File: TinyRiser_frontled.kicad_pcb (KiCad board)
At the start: 4 copper layers, 113.2 x 23.5 mm, 33 parts, among them J2 Bus_PCI_Express_x16, J3 Bus_M.2_Socket_M, J5 Conn_02x04_Odd_Even, M1 Fan_4pin

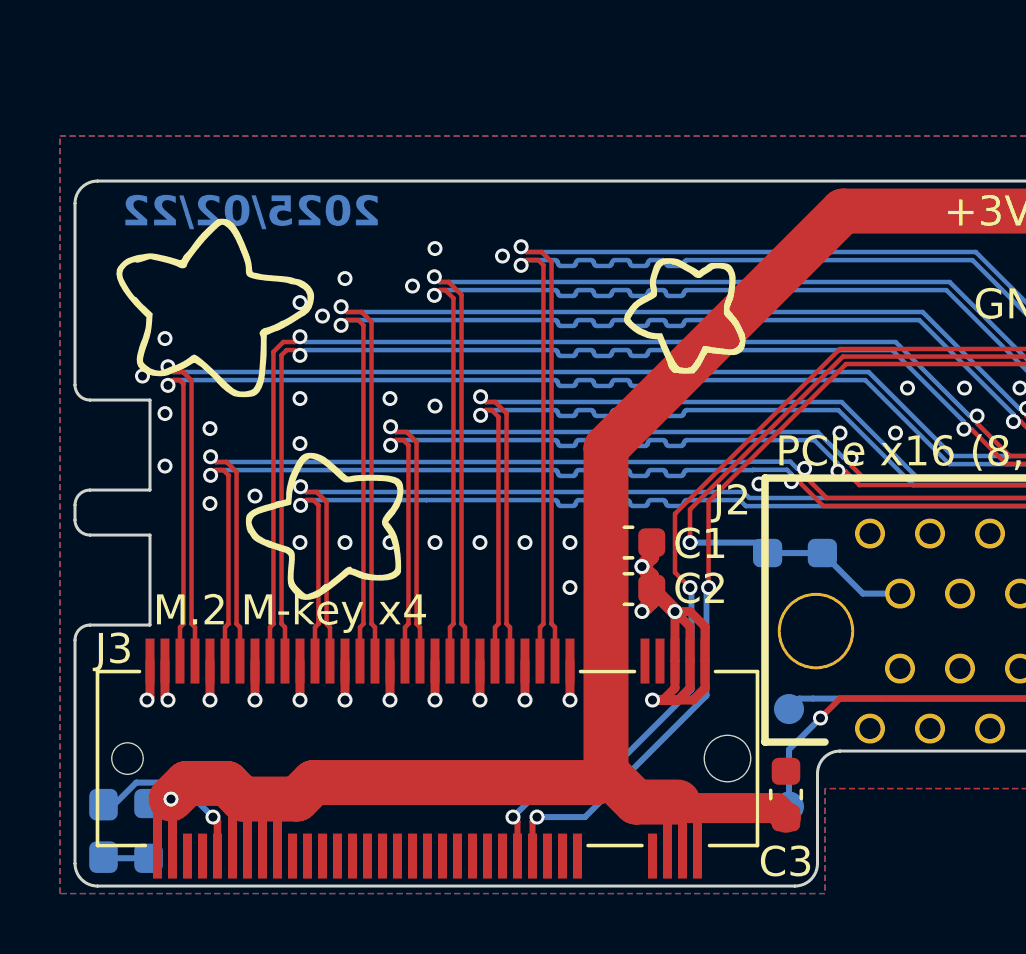
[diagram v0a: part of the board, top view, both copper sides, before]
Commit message: Added alternative version with ssd led on the front for pcba
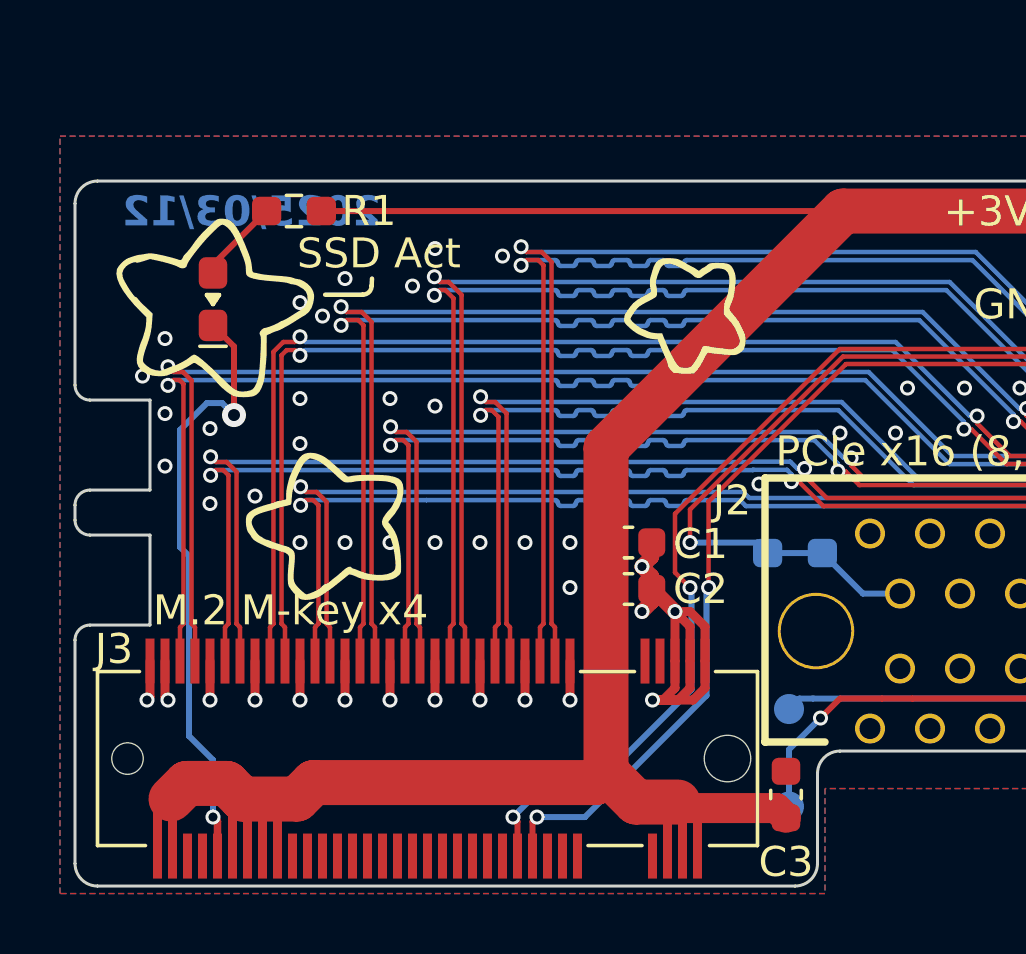
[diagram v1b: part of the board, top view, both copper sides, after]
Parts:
- D1, R1: moved to F.Cu
- moved R1 21.2 mm to (46.3, 120.5), turned to 0 degrees
- moved D1 18.1 mm to (43.6, 123.4), turned to 90 degrees
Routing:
- net +3V3: track 156.8 -> 173.3 mm, vias 1 -> 0
- net Net-(D1-K): track 5.79 -> 20.3 mm, vias 1 -> 2
- net Net-(D1-A): track 1.52 -> 2.80 mm
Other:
- board text added: "2025/03/12"
- board text removed: "2025/02/22"

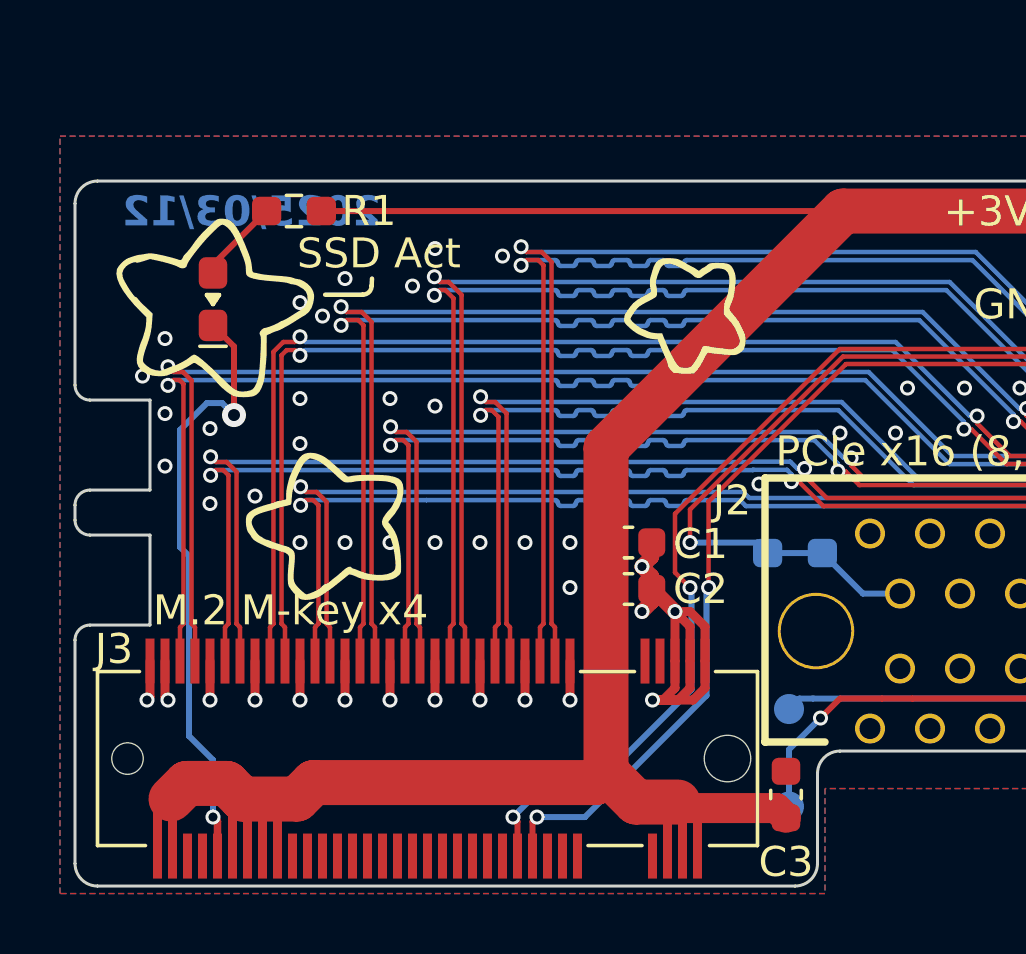
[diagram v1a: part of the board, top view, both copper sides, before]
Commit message: Adjusted frontled via size, trace routing and resistor placement
wow I really did that quick and sloppily last time. I still don't like this version, it looks weird, but it's a little better now at least. Sorry to anyone who already had a stencil made for the previous component placement. I guess you can always order the old version.
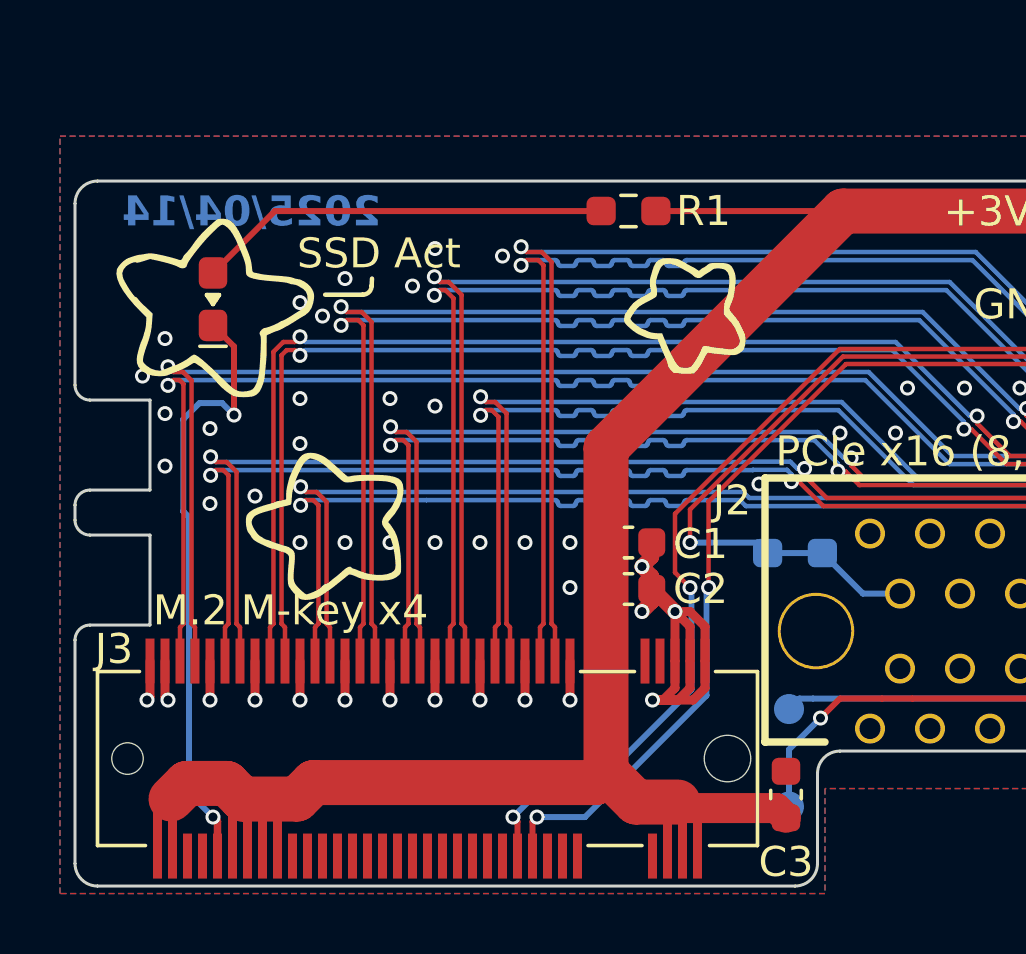
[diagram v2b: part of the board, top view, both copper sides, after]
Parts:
- moved R1 11.2 mm to (57.5, 120.5)
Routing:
- net +3V3: track 173.3 -> 162.2 mm
- net Net-(D1-A): track 2.80 -> 13.8 mm
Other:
- board text added: "2025/04/14"
- board text removed: "2025/03/12"
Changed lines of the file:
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@@
 	(footprint "Resistor_SMD:R_0603_1608Metric_Pad0.98x0.95mm_HandSolder"
 		(layer "F.Cu")
-		(at 46.3 120.5)
+		(at 57.45 120.5)
 		(descr "Resistor SMD 0603 (1608 Metric), square (rectangular) end terminal, IPC_7351 nominal with elongated pad for handsoldering. (Body size source: IPC-SM-782 page 72, https://www.pcb-3d.com/wordpress/wp-content/uploads/ipc-sm-782a_amendment_1_and_2.pdf), generated with kicad-footprint-generator")
 		(tags "resistor handsolder")
@@
 		(layer "User.2")
 	)
-	(gr_text "2025/03/12"
+	(gr_text "2025/04/14"
 		(at 49.2 121.1 0)
 		(layer "B.Cu")
@@
 	)
 	(segment
+		(start 58.3625 120.5)
+		(end 64.6 120.5)
+		(width 0.2)
+		(layer "F.Cu")
+		(net 6)
+	)
+	(segment
 		(start 88.85 120.5)
 		(end 73.3 120.5)
@@
 	)
 	(segment
-		(start 64.6 120.5)
-		(end 47.2125 120.5)
-		(width 0.2)
-		(layer "F.Cu")
-		(net 6)
-	)
-	(segment
 		(start 45.25 142)
 		(end 45.25 140.1)
@@
 	)
 	(segment
-		(start 44.3 127.3)
-		(end 44.3 125.0125)
-		(width 0.2)
-		(layer "F.Cu")
-		(net 62)
-	)
-	(segment
 		(start 43.75 142)
 		(end 43.75 140.85)
@@
 		(net 62)
 	)
+	(segment
+		(start 44.3 125.0125)
+		(end 44.3 127.3)
+		(width 0.2)
+		(layer "F.Cu")
+		(net 62)
+	)
 	(via
 		(at 43.6 140.7)
@@
 	(via
 		(at 44.3 127.3)
-		(size 0.8)
-		(drill 0.4)
+		(size 0.5)
+		(drill 0.3)
 		(layers "F.Cu" "B.Cu")
 		(net 62)
 	)
 	(segment
-		(start 42.8 138)
-		(end 43.6 138.8)
+		(start 44.3 127.3)
+		(end 43.9 126.9)
 		(width 0.2)
 		(layer "B.Cu")
@@
 	)
 	(segment
-		(start 43.6 138.8)
+		(start 42.8 139.9)
 		(end 43.6 140.7)
 		(width 0.2)
@@
 	)
 	(segment
-		(start 42.5 127.8)
-		(end 42.5 131.7)
+		(start 42.61 127.44)
+		(end 42.61 130.515)
 		(width 0.2)
 		(layer "B.Cu")
@@
 	)
 	(segment
-		(start 42.8 132)
-		(end 42.8 138)
-		(width 0.2)
-		(layer "B.Cu")
-		(net 62)
-	)
-	(segment
-		(start 43.4 126.9)
-		(end 42.5 127.8)
+		(start 43.9 126.9)
+		(end 43.15 126.9)
 		(width 0.2)
 		(layer "B.Cu")
@@
 	)
 	(segment
-		(start 44.3 127.3)
-		(end 43.9 126.9)
+		(start 42.61 130.515)
+		(end 42.8 130.705)
 		(width 0.2)
 		(layer "B.Cu")
@@
 	)
 	(segment
-		(start 43.9 126.9)
-		(end 43.4 126.9)
+		(start 43.15 126.9)
+		(end 42.61 127.44)
 		(width 0.2)
 		(layer "B.Cu")
@@
 	)
 	(segment
-		(start 42.5 131.7)
-		(end 42.8 132)
+		(start 42.8 130.705)
+		(end 42.8 139.9)
 		(width 0.2)
 		(layer "B.Cu")
@@
 	)
 	(segment
-		(start 45.3875 120.5)
-		(end 43.6 122.2875)
+		(start 56.5375 120.5)
+		(end 45.6625 120.5)
 		(width 0.2)
 		(layer "F.Cu")
@@
 	)
 	(segment
-		(start 43.6 122.2875)
+		(start 45.6625 120.5)
 		(end 43.6 122.5625)
 		(width 0.2)

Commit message: Added note to frontled version too
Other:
- board text added: "For documentation visit: github.com/a-little-wifi/Tinyriser"
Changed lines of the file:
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@@
+		)
+	)
+	(gr_text "For documentation visit:\ngithub.com/a-little-wifi/Tinyriser"
+		(at 84.5 130.1 0)
+		(layer "B.SilkS")
+		(effects
+			(font
+				(size 0.66 0.66)
+				(thickness 0.12)
+				(bold yes)
+			)
+			(justify left bottom mirror)
 		)
 	)
